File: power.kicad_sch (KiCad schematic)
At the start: 18 parts, among them U3 LM2586S

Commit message: Updated references after merging
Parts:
- renumbered C5 to C1, C1 to C3, C3 to C4, C4 to C5, TP2 to GND, TP1 to HV_OUT, R5 to R1, R4 to R2, R12 to R3, R13 to R4, R2 to R5, R1 to R6, R3 to R7, U3 to U1, Ue to Ue1
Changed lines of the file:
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@@
 		(on_board yes)
 		(dnp no)
-		(property "Reference" "R12"
+		(property "Reference" "R3"
 			(at 160.02 93.9799 0)
 			(effects
@@
 			(project "FES_Hardware"
 				(path "/225cfa82-97e7-4320-90e1-4d94ef39f9f2/9d03af3c-7e27-487a-be84-d59389aa1574"
-					(reference "R12")
+					(reference "R3")
 					(unit 1)
 				)
@@
 		(dnp no)
 		(fields_autoplaced yes)
-		(property "Reference" "TP2"
+		(property "Reference" "GND"
 			(at 162.56 119.3799 90)
 			(effects
@@
 			(project "FES_Hardware"
 				(path "/225cfa82-97e7-4320-90e1-4d94ef39f9f2/9d03af3c-7e27-487a-be84-d59389aa1574"
-					(reference "TP2")
+					(reference "GND")
 					(unit 1)
 				)
@@
 		(on_board yes)
 		(dnp no)
-		(property "Reference" "C1"
+		(property "Reference" "C3"
 			(at 137.16 68.9609 0)
 			(effects
@@
 			(project "FES_Hardware"
 				(path "/225cfa82-97e7-4320-90e1-4d94ef39f9f2/9d03af3c-7e27-487a-be84-d59389aa1574"
-					(reference "C1")
+					(reference "C3")
 					(unit 1)
 				)
@@
 		(dnp no)
 		(fields_autoplaced yes)
-		(property "Reference" "#PWR08"
+		(property "Reference" "#PWR011"
 			(at 218.44 119.38 0)
 			(effects
@@
 			(project "FES_Hardware"
 				(path "/225cfa82-97e7-4320-90e1-4d94ef39f9f2/9d03af3c-7e27-487a-be84-d59389aa1574"
-					(reference "#PWR08")
+					(reference "#PWR011")
 					(unit 1)
 				)
@@
 		(dnp no)
 		(fields_autoplaced yes)
-		(property "Reference" "#PWR09"
+		(property "Reference" "#PWR013"
 			(at 226.06 123.19 0)
 			(effects
@@
 			(project "FES_Hardware"
 				(path "/225cfa82-97e7-4320-90e1-4d94ef39f9f2/9d03af3c-7e27-487a-be84-d59389aa1574"
-					(reference "#PWR09")
+					(reference "#PWR013")
 					(unit 1)
 				)
@@
 		(dnp no)
 		(fields_autoplaced yes)
-		(property "Reference" "R13"
+		(property "Reference" "R4"
 			(at 160.02 110.4899 0)
 			(effects
@@
 			(project "FES_Hardware"
 				(path "/225cfa82-97e7-4320-90e1-4d94ef39f9f2/9d03af3c-7e27-487a-be84-d59389aa1574"
-					(reference "R13")
+					(reference "R4")
 					(unit 1)
 				)
@@
 		(on_board yes)
 		(dnp no)
-		(property "Reference" "Ue"
+		(property "Reference" "Ue1"
 			(at 197.6311 92.71 0)
 			(effects
@@
 			(project ""
 				(path "/225cfa82-97e7-4320-90e1-4d94ef39f9f2/9d03af3c-7e27-487a-be84-d59389aa1574"
-					(reference "Ue")
+					(reference "Ue1")
 					(unit 1)
 				)
@@
 		(on_board yes)
 		(dnp no)
-		(property "Reference" "R4"
+		(property "Reference" "R2"
 			(at 83.82 125.7299 0)
 			(effects
@@
 			(project "FES_Hardware"
 				(path "/225cfa82-97e7-4320-90e1-4d94ef39f9f2/9d03af3c-7e27-487a-be84-d59389aa1574"
-					(reference "R4")
+					(reference "R2")
 					(unit 1)
 				)
@@
 		(dnp no)
 		(fields_autoplaced yes)
-		(property "Reference" "#PWR07"
+		(property "Reference" "#PWR08"
 			(at 157.48 129.54 0)
 			(effects
@@
 			(project "FES_Hardware"
 				(path "/225cfa82-97e7-4320-90e1-4d94ef39f9f2/9d03af3c-7e27-487a-be84-d59389aa1574"
-					(reference "#PWR07")
+					(reference "#PWR08")
 					(unit 1)
 				)
@@
 		(dnp no)
 		(fields_autoplaced yes)
-		(property "Reference" "#PWR011"
+		(property "Reference" "#PWR04"
 			(at 86.36 148.59 0)
 			(effects
@@
 			(project "FES_Hardware"
 				(path "/225cfa82-97e7-4320-90e1-4d94ef39f9f2/9d03af3c-7e27-487a-be84-d59389aa1574"
-					(reference "#PWR011")
+					(reference "#PWR04")
 					(unit 1)
 				)
@@
 		(on_board yes)
 		(dnp no)
-		(property "Reference" "R5"
+		(property "Reference" "R1"
 			(at 64.77 104.1399 0)
 			(effects
@@
 			(project "FES_Hardware"
 				(path "/225cfa82-97e7-4320-90e1-4d94ef39f9f2/9d03af3c-7e27-487a-be84-d59389aa1574"
-					(reference "R5")
+					(reference "R1")
 					(unit 1)
 				)
@@
 		(dnp no)
 		(fields_autoplaced yes)
-		(property "Reference" "U3"
+		(property "Reference" "U1"
 			(at 84.7441 87.63 0)
 			(effects
@@
 			(project ""
 				(path "/225cfa82-97e7-4320-90e1-4d94ef39f9f2/9d03af3c-7e27-487a-be84-d59389aa1574"
-					(reference "U3")
+					(reference "U1")
 					(unit 1)
 				)
@@
 		(dnp no)
 		(fields_autoplaced yes)
-		(property "Reference" "#PWR04"
+		(property "Reference" "#PWR07"
 			(at 148.59 85.09 0)
 			(effects
@@
 			(project "FES_Hardware"
 				(path "/225cfa82-97e7-4320-90e1-4d94ef39f9f2/9d03af3c-7e27-487a-be84-d59389aa1574"
-					(reference "#PWR04")
+					(reference "#PWR07")
 					(unit 1)
 				)
@@
 		(dnp no)
 		(fields_autoplaced yes)
-		(property "Reference" "#PWR02"
+		(property "Reference" "#PWR06"
 			(at 91.44 128.27 0)
 			(effects
@@
 			(project "FES_Hardware"
 				(path "/225cfa82-97e7-4320-90e1-4d94ef39f9f2/9d03af3c-7e27-487a-be84-d59389aa1574"
-					(reference "#PWR02")
+					(reference "#PWR06")
 					(unit 1)
 				)
@@
 		(dnp no)
 		(fields_autoplaced yes)
-		(property "Reference" "#PWR010"
+		(property "Reference" "#PWR012"
 			(at 219.71 92.71 0)
 			(effects
@@
 			(project "FES_Hardware"
 				(path "/225cfa82-97e7-4320-90e1-4d94ef39f9f2/9d03af3c-7e27-487a-be84-d59389aa1574"
-					(reference "#PWR010")
+					(reference "#PWR012")
 					(unit 1)
 				)
@@
 		(on_board yes)
 		(dnp no)
-		(property "Reference" "R3"
+		(property "Reference" "R7"
 			(at 231.14 95.2499 0)
 			(effects
@@
 			(project "FES_Hardware"
 				(path "/225cfa82-97e7-4320-90e1-4d94ef39f9f2/9d03af3c-7e27-487a-be84-d59389aa1574"
-					(reference "R3")
+					(reference "R7")
 					(unit 1)
 				)
@@
 		(dnp no)
 		(fields_autoplaced yes)
-		(property "Reference" "C3"
+		(property "Reference" "C4"
 			(at 152.4 68.9609 0)
 			(effects
@@
 			(project ""
 				(path "/225cfa82-97e7-4320-90e1-4d94ef39f9f2/9d03af3c-7e27-487a-be84-d59389aa1574"
-					(reference "C3")
+					(reference "C4")
 					(unit 1)
 				)
@@
 		(dnp no)
 		(fields_autoplaced yes)
-		(property "Reference" "#PWR03"
+		(property "Reference" "#PWR010"
 			(at 181.61 99.06 0)
 			(effects
@@
 			(project "FES_Hardware"
 				(path "/225cfa82-97e7-4320-90e1-4d94ef39f9f2/9d03af3c-7e27-487a-be84-d59389aa1574"
-					(reference "#PWR03")
+					(reference "#PWR010")
 					(unit 1)
 				)
@@
 		(on_board yes)
 		(dnp no)
-		(property "Reference" "C4"
+		(property "Reference" "C5"
 			(at 185.42 86.3599 0)
 			(effects
@@
 			(project "FES_Hardware"
 				(path "/225cfa82-97e7-4320-90e1-4d94ef39f9f2/9d03af3c-7e27-487a-be84-d59389aa1574"
-					(reference "C4")
+					(reference "C5")
 					(unit 1)
 				)
@@
 		(on_board yes)
 		(dnp no)
-		(property "Reference" "R1"
+		(property "Reference" "R6"
 			(at 228.6 110.4899 0)
 			(effects
@@
 			(project "FES_Hardware"
 				(path "/225cfa82-97e7-4320-90e1-4d94ef39f9f2/9d03af3c-7e27-487a-be84-d59389aa1574"
-					(reference "R1")
+					(reference "R6")
 					(unit 1)
 				)
@@
 		(dnp no)
 		(fields_autoplaced yes)
-		(property "Reference" "C5"
+		(property "Reference" "C1"
 			(at 90.17 134.6199 0)
 			(effects
@@
 			(project "FES_Hardware"
 				(path "/225cfa82-97e7-4320-90e1-4d94ef39f9f2/9d03af3c-7e27-487a-be84-d59389aa1574"
-					(reference "C5")
+					(reference "C1")
 					(unit 1)
 				)
@@
 		(dnp no)
 		(fields_autoplaced yes)
-		(property "Reference" "#PWR06"
+		(property "Reference" "#PWR09"
 			(at 176.53 83.82 0)
 			(effects
@@
 			(project "FES_Hardware"
 				(path "/225cfa82-97e7-4320-90e1-4d94ef39f9f2/9d03af3c-7e27-487a-be84-d59389aa1574"
-					(reference "#PWR06")
+					(reference "#PWR09")
 					(unit 1)
 				)
@@
 		(dnp no)
 		(fields_autoplaced yes)
-		(property "Reference" "#PWR012"
+		(property "Reference" "#PWR02"
 			(at 62.23 119.38 0)
 			(effects
@@
 			(project "FES_Hardware"
 				(path "/225cfa82-97e7-4320-90e1-4d94ef39f9f2/9d03af3c-7e27-487a-be84-d59389aa1574"
-					(reference "#PWR012")
+					(reference "#PWR02")
 					(unit 1)
 				)
@@
 		(dnp no)
 		(fields_autoplaced yes)
-		(property "Reference" "#PWR014"
+		(property "Reference" "#PWR03"
 			(at 81.28 124.46 0)
 			(effects
@@
 			(project "FES_Hardware"
 				(path "/225cfa82-97e7-4320-90e1-4d94ef39f9f2/9d03af3c-7e27-487a-be84-d59389aa1574"
-					(reference "#PWR014")
+					(reference "#PWR03")
 					(unit 1)
 				)
@@
 		(on_board yes)
 		(dnp no)
-		(property "Reference" "R2"
+		(property "Reference" "R5"
 			(at 222.25 95.2499 0)
 			(effects
@@
 			(project "FES_Hardware"
 				(path "/225cfa82-97e7-4320-90e1-4d94ef39f9f2/9d03af3c-7e27-487a-be84-d59389aa1574"
-					(reference "R2")
+					(reference "R5")
 					(unit 1)
 				)
@@
 		(dnp no)
 		(fields_autoplaced yes)
-		(property "Reference" "TP1"
+		(property "Reference" "HV_OUT"
 			(at 156.21 55.1179 0)
 			(effects
@@
 			(project ""
 				(path "/225cfa82-97e7-4320-90e1-4d94ef39f9f2/9d03af3c-7e27-487a-be84-d59389aa1574"
-					(reference "TP1")
-					(unit 1)
-				)
+					(reference "HV_OUT")
+					(unit 1)
+				)

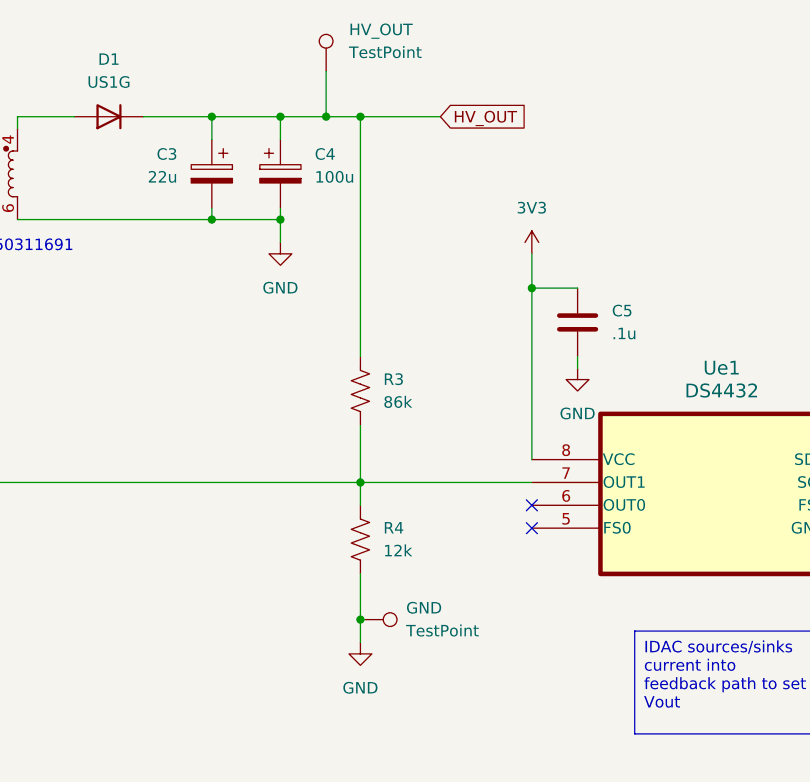
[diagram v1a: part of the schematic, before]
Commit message: Updated footprints of passive elements to be 0805 Hand-Solder
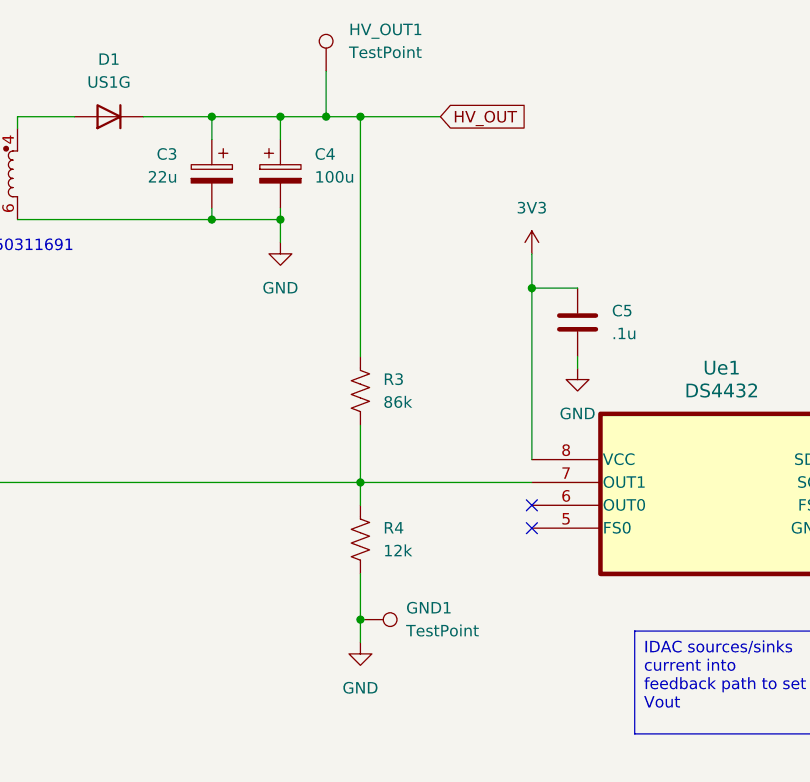
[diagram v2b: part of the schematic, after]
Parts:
- C1, C2, C3, C4, C5: footprint (none) -> Capacitor_SMD:C_0805_2012Metric_Pad1.18x1.45mm_HandSolder
- GND1: renamed from GND; footprint (none) -> TestPoint:TestPoint_Keystone_5019_Minature
- HV_OUT1: renamed from HV_OUT; footprint (none) -> TestPoint:TestPoint_Keystone_5019_Minature
- R1, R2, R3, R4, R5, R6, R7: footprint (none) -> Resistor_SMD:R_0805_2012Metric_Pad1.20x1.40mm_HandSolder
- U1: footprint TS7B -> FES_Footprints:TS7B
- Ue1: footprint 21-0036_U8+1_MXM -> FES_Footprints:21-0036_U8&plus_1_MXM
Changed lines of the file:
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@@
 			)
 		)
-		(property "Footprint" ""
+		(property "Footprint" "Resistor_SMD:R_0805_2012Metric_Pad1.20x1.40mm_HandSolder"
 			(at 158.496 95.504 90)
 			(effects
@@
 		(dnp no)
 		(fields_autoplaced yes)
-		(property "Reference" "GND"
+		(property "Reference" "GND1"
 			(at 162.56 119.3799 90)
 			(effects
@@
 			)
 		)
-		(property "Footprint" ""
+		(property "Footprint" "TestPoint:TestPoint_Keystone_5019_Minature"
 			(at 157.48 125.73 0)
 			(effects
@@
 			(project "FES_Hardware"
 				(path "/225cfa82-97e7-4320-90e1-4d94ef39f9f2/9d03af3c-7e27-487a-be84-d59389aa1574"
-					(reference "GND")
+					(reference "GND1")
 					(unit 1)
 				)
@@
 			)
 		)
-		(property "Footprint" ""
+		(property "Footprint" "Capacitor_SMD:C_0805_2012Metric_Pad1.18x1.45mm_HandSolder"
 			(at 140.0048 74.93 0)
 			(effects
@@
 			)
 		)
-		(property "Footprint" ""
+		(property "Footprint" "Resistor_SMD:R_0805_2012Metric_Pad1.20x1.40mm_HandSolder"
 			(at 158.496 112.014 90)
 			(effects
@@
 			)
 		)
-		(property "Footprint" "21-0036_U8+1_MXM"
+		(property "Footprint" "FES_Footprints:21-0036_U8&plus_1_MXM"
 			(at 217.17 102.87 0)
 			(effects
@@
 			)
 		)
-		(property "Footprint" ""
+		(property "Footprint" "Resistor_SMD:R_0805_2012Metric_Pad1.20x1.40mm_HandSolder"
 			(at 85.344 127.254 90)
 			(effects
@@
 			)
 		)
-		(property "Footprint" ""
+		(property "Footprint" "Resistor_SMD:R_0805_2012Metric_Pad1.20x1.40mm_HandSolder"
 			(at 63.246 105.664 90)
 			(effects
@@
 			)
 		)
-		(property "Footprint" "TS7B"
+		(property "Footprint" "FES_Footprints:TS7B"
 			(at 62.23 97.79 0)
 			(effects
@@
 			)
 		)
-		(property "Footprint" ""
+		(property "Footprint" "Resistor_SMD:R_0805_2012Metric_Pad1.20x1.40mm_HandSolder"
 			(at 229.616 96.774 90)
 			(effects
@@
 			)
 		)
-		(property "Footprint" ""
+		(property "Footprint" "Capacitor_SMD:C_0805_2012Metric_Pad1.18x1.45mm_HandSolder"
 			(at 149.5552 74.93 0)
 			(effects
@@
 			)
 		)
-		(property "Footprint" ""
+		(property "Footprint" "Capacitor_SMD:C_0805_2012Metric_Pad1.18x1.45mm_HandSolder"
 			(at 182.5752 91.44 0)
 			(effects
@@
 			)
 		)
-		(property "Footprint" ""
+		(property "Footprint" "Capacitor_SMD:C_0805_2012Metric_Pad1.18x1.45mm_HandSolder"
 			(at 91.1352 77.47 0)
 			(effects
@@
 			)
 		)
-		(property "Footprint" ""
+		(property "Footprint" "Resistor_SMD:R_0805_2012Metric_Pad1.20x1.40mm_HandSolder"
 			(at 227.076 112.014 90)
 			(effects
@@
 			)
 		)
-		(property "Footprint" ""
+		(property "Footprint" "Capacitor_SMD:C_0805_2012Metric_Pad1.18x1.45mm_HandSolder"
 			(at 87.3252 139.7 0)
 			(effects
@@
 			)
 		)
-		(property "Footprint" ""
+		(property "Footprint" "Resistor_SMD:R_0805_2012Metric_Pad1.20x1.40mm_HandSolder"
 			(at 220.726 96.774 90)
 			(effects
@@
 		(dnp no)
 		(fields_autoplaced yes)
-		(property "Reference" "HV_OUT"
+		(property "Reference" "HV_OUT1"
 			(at 156.21 55.1179 0)
 			(effects
@@
 			)
 		)
-		(property "Footprint" ""
+		(property "Footprint" "TestPoint:TestPoint_Keystone_5019_Minature"
 			(at 158.75 59.69 0)
 			(effects
@@
 			(project ""
 				(path "/225cfa82-97e7-4320-90e1-4d94ef39f9f2/9d03af3c-7e27-487a-be84-d59389aa1574"
-					(reference "HV_OUT")
-					(unit 1)
-				)
+					(reference "HV_OUT1")
+					(unit 1)
+				)

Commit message: added transformer and NMOS footprints
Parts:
- L1: footprint (none) -> FES_Footprints:WE 750311691
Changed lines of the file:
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@@
 			)
 		)
-		(property "Footprint" ""
+		(property "Footprint" "FES_Footprints:WE 750311691"
 			(at 116.84 71.12 0)
 			(effects
